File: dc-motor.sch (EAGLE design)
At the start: 60 parts, among them IC1 MEGA8-P, X3 RIA_3POL, X4 RIA_3POL, X5 RIA_2POL, X6 JUMP1-4

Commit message: Schaltplan Fertig
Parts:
- added C15, C16: 15pF, Capacitor:C-BELAB0805
- added H3: MOUNT-HOLE3.2, Holes:MOUNT-HOLE3.2
- added R24, R28, R31, R32: 2k2, Resistor:0805
- added R25, R26, R29, R30: 10R, Resistor:0805
- added R27: 180R, Resistor:0805
- added R33, R34, R35: 2k7, Resistor:0805
- added U$34: ACPL-247, Optoelectronic:ACPL-247
- added U$35, U$38: IRF7341, Transistor:IRF7341
- added X7, X8: PFVERB10, Connector:PFVERB10
- C11: value 1µF -> 100nF
- IC1: value MEGA8-P -> MEGA32-A; device atmel:MEGA8-P -> atmel:MEGA32-A; MPN (none) -> ATMEGA32-16AU; OC_FARNELL (none) -> 9171274; OC_NEWARK (none) -> 69K6677
- R13: value 3,3k -> 2k7
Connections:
- removed net N$14 (its old number): IC1.PC0(ADC0), U$17.OUT
- removed net N$22: IC1.PC6(/RESET), S1.S, S1.S1
- removed net N$30: IC1.PC2(ADC2)
- removed net N$32 (its old number): R21.1, U$3.PHASE
- removed net N$39: IC1.PD4(XCK/T0), R19.1
- removed net N$40: IC1.PD3(INT1), R18.2
- removed net N$41: R17.2
- removed net N$51: IC1.PC3(ADC3)
- removed net N$52: IC1.PC4(ADC4/SDA)
- removed net N$53: IC1.PC5(ADC5/SCL)
- new net ENDLAGE_A: IC1.(T1)PB1, R32.1, U$35G$1.N-G1
- new net ENDLAGE_B: IC1.(T0/XCK)PB0, R31.1, U$35G$2.N-G1
- new net FAEHRTNACHA: IC1.(ADC1)PA1, X7.5.1
- new net FAEHRTNACHB: IC1.(ADC2)PA2, X7.6.1
- new net LOCAL/REMOTE: IC1.(ADC4)PA4, X7.8.1
- new net MISO: IC1.(MISO)PB6, R18.2, X8.3.1
- new net MOSI: IC1.(MOSI)PB5, R19.1, X8.9.1
- new net MOTORSICHERUNGLED: IC1.(ADC0)PA0, X7.4.1
- new net MOTORSTOP: IC1.(ADC3)PA3, X7.7.1
- new net N$10: IC1.(ADC6)PA6, U$17.OUT
- new net N$23: IC1.(AIN1/OC0)PB3, R28.1, U$38G$2.N-G1
- new net N$37: U$34G$2.COL, X2.5
- new net N$54: R26.2, X2.4
- new net N$55: R25.2, X2.3
- new net N$57: U$34G$2.A
- new net N$58: U$34G$2.EMIT, U$38G$1.N-S1, U$38G$2.N-S1
- new net N$59: R25.1, U$38G$2.D1
- new net N$61: R27.2, U$34G$2.C
- new net N$62: R26.1, U$38G$1.D1
- new net N$67: R29.1, X3.1.STIFT
- new net N$68: R30.1, X4.1.STIFT
- new net N$69: R30.2, U$35G$2.D1
- new net N$70: U$35G$2.N-S1, X4.2.STIFT
- new net N$71: R29.2, U$35G$1.D1
- new net N$72: U$35G$1.N-S1, X3.2.STIFT
- new net N$77: R21.1, R35.2, U$3.PHASE
- new net RESET: IC1.RESET, S1.S, S1.S1, X8.6.1
- new net SCK: IC1.(SCK)PB7, R17.2, X8.1.1
- net +24V: now also X7.3.1
- net GND: now also C15.2, C16.2, C3.1, IC1.GND1, IC1.GND2, R13.1, R24.2, R27.1, R28.2, R31.2, R32.2, R33.1, R34.1, R35.1, X3.3.STIFT, X4.3.STIFT, X7.10.1, X8.10.1, X8.2.1
- net N$11: now also IC1.(TMS)PC3; no longer IC1.PB4(MISO)
- net N$15: now also IC1.(TDO)PC4; no longer IC1.PB3(MOSI/OC2)
- net N$16: now also IC1.(AIN0/INT2)PB2, R24.1, U$38G$1.N-G1; no longer C3.1
- net N$17: now also IC1.(TDI)PC5; no longer IC1.PB2(SS/OC1B)
- net N$18: now also IC1.(TOSC1)PC6; no longer IC1.PB1(OC1A)
- net N$19: now also X7.1.1
- net N$2: now also C15.1, G1.1, IC1.XTAL1; no longer G1.2, IC1.PB6(XTAL1/TOSC1)
- net N$20: now also X7.2.1
- net N$21: now also C9.2
- net N$25: now also IC1.(TOSC2)PC7; no longer IC1.PB0(ICP)
- net N$3: now also C16.1, G1.2, IC1.XTAL2; no longer G1.1, IC1.PB7(XTAL2/TOSC2)
- net N$31: now also R34.2
- net N$34: now also R13.2; no longer R13.1
- net N$35: now also R22.2
- net N$38: now also IC1.(SS)PB4; no longer IC1.PD5(T1)
- net N$4: now also IC1.(RXD)PD0; no longer IC1.PD0(RXD)
- net N$48: now also R33.2
- net N$50: now also IC1.(ADC5)PA5; no longer IC1.PC1(ADC1)
- net N$6: now also IC1.(ADC7)PA7
- net N$8: now also IC1.(TXD)PD1; no longer IC1.PD1(TXD)
- net N$9: now also IC1.(TCK)PC2; no longer IC1.PB5(SCK)
- net VDD: now also IC1.VCC, IC1.VCC1, IC1.VCC2, X7.9.1, X8.4.1; no longer IC1.VCC@1, R13.2
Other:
- note added: "Auswertung Endlage A"
- note added: "Auswertung Endlage B"
- note added: "Endschalter A"
- note added: "Endschalter B"
- note added: "Fährt nach A"
- note added: "Fährt nach B"
- note added: "Local/Remote"
- note added: "Motor Sicherung LED"
- note added: "Motorstop"
- moved on the sheet: C10, C2, C3, C4, C7, C8, C9, F1, G1, H1, H2, R10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

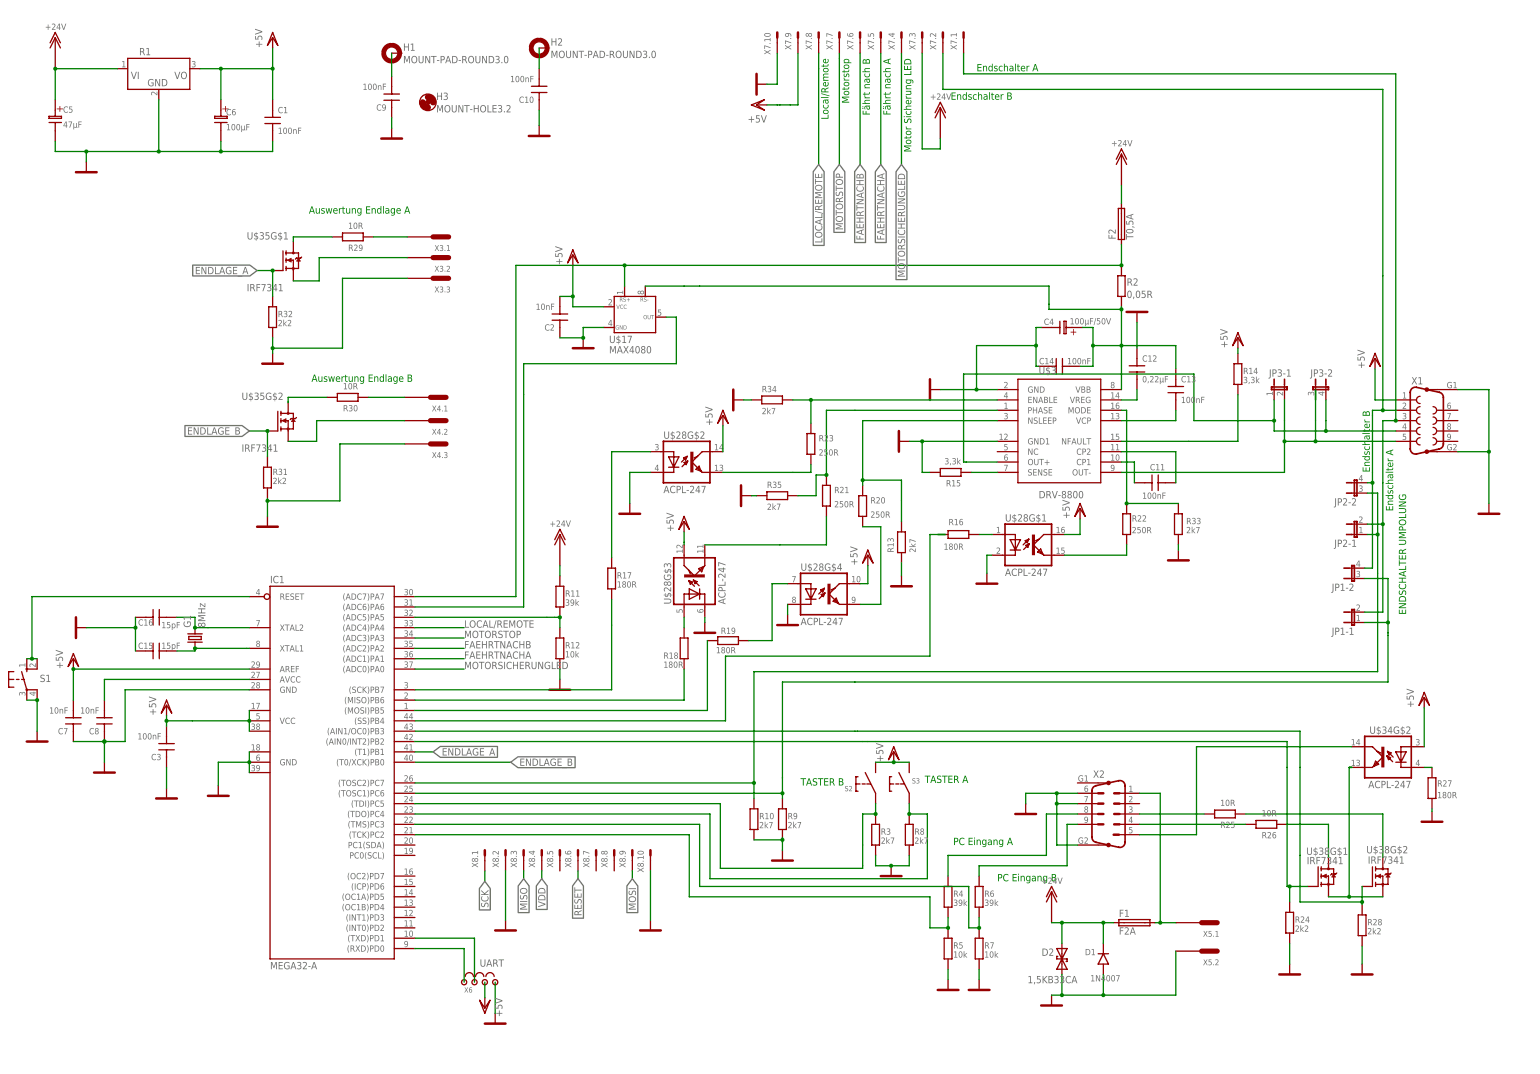
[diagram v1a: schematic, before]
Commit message: Schaltplan Verbessert und mit dem Layout begonnen
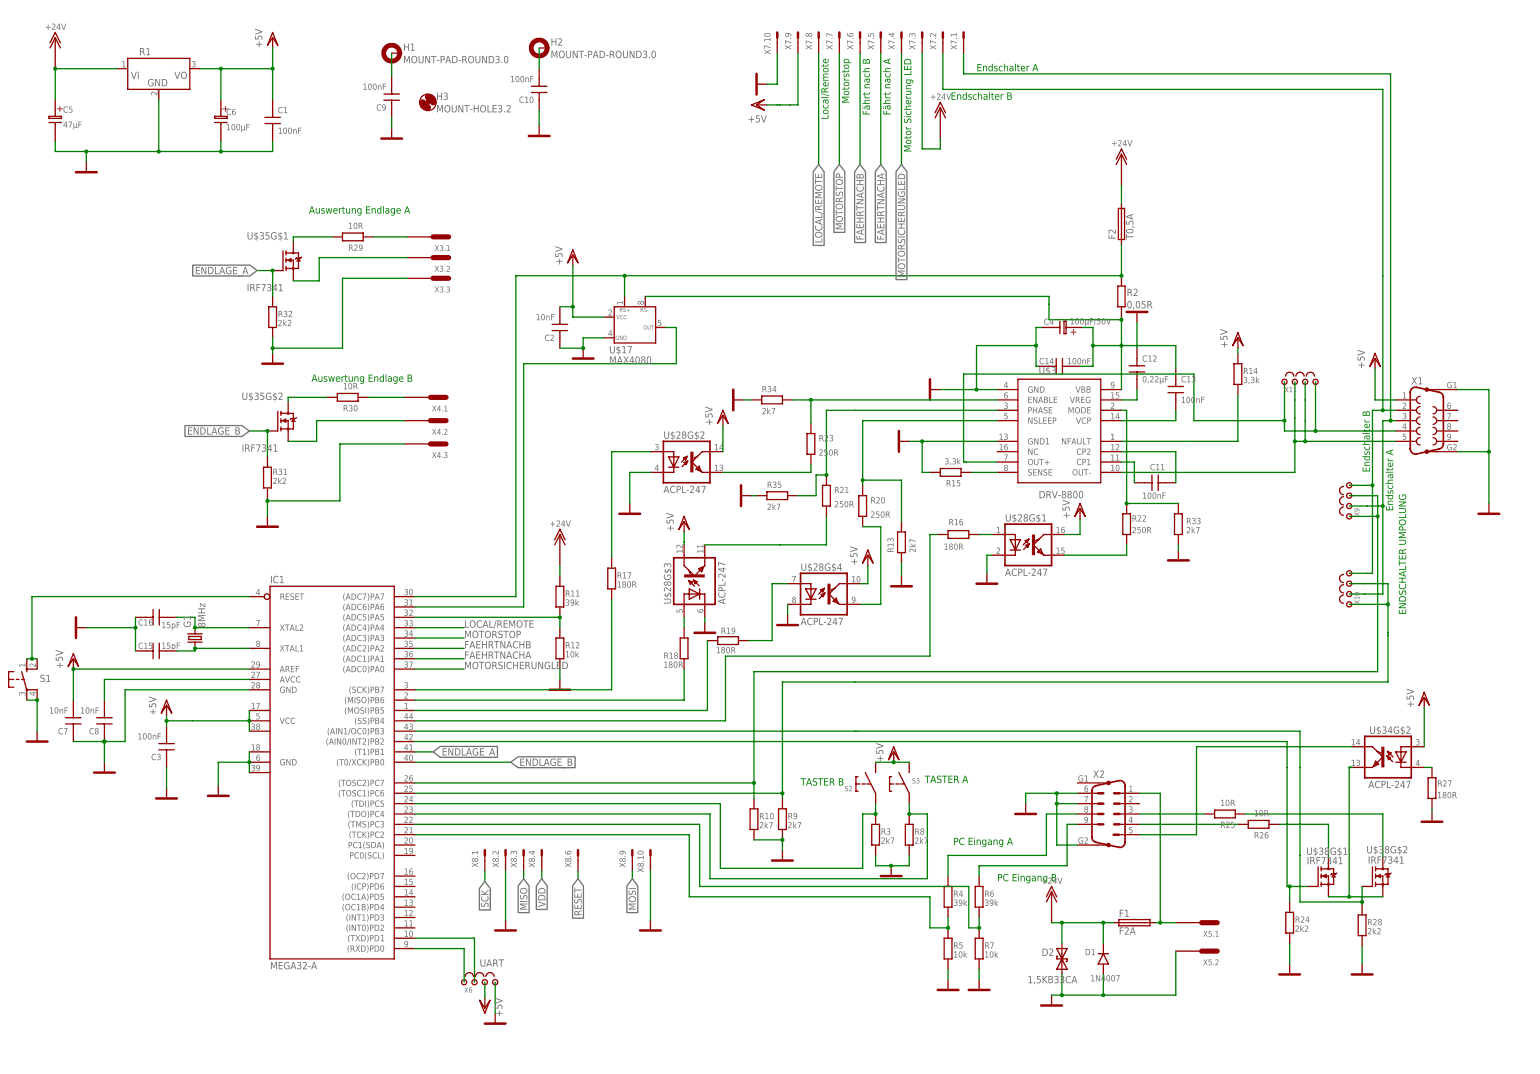
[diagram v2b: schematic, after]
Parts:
- removed JP1, JP2, JP3: (no value), jumper:JP2QE
- added X10, X11, X9: JUMP1-4, Connector:JUMP1-4
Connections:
- removed net N$19 (its old number): JP1-1.2, JP2-1.2, X1.3, X7.1.1
- removed net N$57: U$34G$2.A
- removed net N$7: JP3-1.2, JP3-2.1, U$3.OUT-, X1.5
- new net N$22: X1.3, X10.2, X7.1.1, X9.2
- new net N$30: U$3.OUT-, X1.5, X11.2, X11.3
- net N$18: now also X10.1, X10.3; no longer JP1-1.1, JP1-2.1
- net N$20: now also X10.4, X9.4; no longer JP1-2.2, JP2-2.2
- net N$25: now also X9.1, X9.3; no longer JP2-1.1, JP2-2.1
- net N$5: now also X11.1, X11.4; no longer JP3-1.1, JP3-2.2
- net VDD: now also U$34G$2.A
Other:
- moved on the sheet: C2, R2, R26, U$17

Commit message: Schaltplan erweitert
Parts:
- G1: device Crystals:CRYTAL -> Crystals:CRYTALHC18U-V
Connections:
- net N$6: no longer IC1.(ADC7)PA7
- net VDD: now also IC1.(ADC7)PA7
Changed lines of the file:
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@@
 <setting verticaltext="up"/>
 </settings>
-<grid distance="0.635" unitdist="mm" unit="mm" style="lines" multiple="1" display="yes" altdistance="0.3175" altunitdist="mm" altunit="mm"/>
+<grid distance="0.635" unitdist="mm" unit="mm" style="dots" multiple="1" display="yes" altdistance="0.3175" altunitdist="mm" altunit="mm"/>
 <layers>
-<layer number="1" name="Top" color="4" fill="1" visible="yes" active="no"/>
-<layer number="2" name="Route2" color="1" fill="3" visible="yes" active="no"/>
-<layer number="3" name="Route3" color="4" fill="3" visible="yes" active="no"/>
-<layer number="4" name="Route4" color="1" fill="4" visible="yes" active="no"/>
-<layer number="5" name="Route5" color="4" fill="4" visible="yes" active="no"/>
-<layer number="6" name="Route6" color="1" fill="8" visible="yes" active="no"/>
-<layer number="7" name="Route7" color="4" fill="8" visible="yes" active="no"/>
-<layer number="8" name="Route8" color="1" fill="2" visible="yes" active="no"/>
-<layer number="9" name="Route9" color="4" fill="2" visible="yes" active="no"/>
-<layer number="10" name="Route10" color="1" fill="7" visible="yes" active="no"/>
-<layer number="11" name="Route11" color="4" fill="7" visible="yes" active="no"/>
-<layer number="12" name="Route12" color="1" fill="5" visible="yes" active="no"/>
-<layer number="13" name="Route13" color="4" fill="5" visible="yes" active="no"/>
-<layer number="14" name="Route14" color="1" fill="6" visible="yes" active="no"/>
-<layer number="15" name="Route15" color="4" fill="6" visible="yes" active="no"/>
-<layer number="16" name="Bottom" color="1" fill="1" visible="yes" active="no"/>
-<layer number="17" name="Pads" color="2" fill="1" visible="yes" active="no"/>
-<layer number="18" name="Vias" color="2" fill="1" visible="yes" active="no"/>
-<layer number="19" name="Unrouted" color="6" fill="1" visible="yes" active="no"/>
-<layer number="20" name="Dimension" color="15" fill="1" visible="yes" active="no"/>
-<layer number="21" name="tPlace" color="7" fill="1" visible="yes" active="no"/>
-<layer number="22" name="bPlace" color="7" fill="1" visible="yes" active="no"/>
-<layer number="23" name="tOrigins" color="15" fill="1" visible="yes" active="no"/>
-<layer number="24" name="bOrigins" color="15" fill="1" visible="yes" active="no"/>
-<layer number="25" name="tNames" color="7" fill="1" visible="yes" active="no"/>
-<layer number="26" name="bNames" color="7" fill="1" visible="yes" active="no"/>
-<layer number="27" name="tValues" color="7" fill="1" visible="yes" active="no"/>
-<layer number="28" name="bValues" color="7" fill="1" visible="yes" active="no"/>
+<layer number="1" name="Top" color="4" fill="1" visible="no" active="no"/>
+<layer number="2" name="Route2" color="1" fill="3" visible="no" active="no"/>
+<layer number="3" name="Route3" color="4" fill="3" visible="no" active="no"/>
+<layer number="4" name="Route4" color="1" fill="4" visible="no" active="no"/>
+<layer number="5" name="Route5" color="4" fill="4" visible="no" active="no"/>
+<layer number="6" name="Route6" color="1" fill="8" visible="no" active="no"/>
+<layer number="7" name="Route7" color="4" fill="8" visible="no" active="no"/>
+<layer number="8" name="Route8" color="1" fill="2" visible="no" active="no"/>
+<layer number="9" name="Route9" color="4" fill="2" visible="no" active="no"/>
+<layer number="10" name="Route10" color="1" fill="7" visible="no" active="no"/>
+<layer number="11" name="Route11" color="4" fill="7" visible="no" active="no"/>
+<layer number="12" name="Route12" color="1" fill="5" visible="no" active="no"/>
+<layer number="13" name="Route13" color="4" fill="5" visible="no" active="no"/>
+<layer number="14" name="Route14" color="1" fill="6" visible="no" active="no"/>
+<layer number="15" name="Route15" color="4" fill="6" visible="no" active="no"/>
+<layer number="16" name="Bottom" color="1" fill="1" visible="no" active="no"/>
+<layer number="17" name="Pads" color="2" fill="1" visible="no" active="no"/>
+<layer number="18" name="Vias" color="2" fill="1" visible="no" active="no"/>
+<layer number="19" name="Unrouted" color="6" fill="1" visible="no" active="no"/>
+<layer number="20" name="Dimension" color="15" fill="1" visible="no" active="no"/>
+<layer number="21" name="tPlace" color="7" fill="1" visible="no" active="no"/>
+<layer number="22" name="bPlace" color="7" fill="1" visible="no" active="no"/>
+<layer number="23" name="tOrigins" color="15" fill="1" visible="no" active="no"/>
+<layer number="24" name="bOrigins" color="15" fill="1" visible="no" active="no"/>
+<layer number="25" name="tNames" color="7" fill="1" visible="no" active="no"/>
+<layer number="26" name="bNames" color="7" fill="1" visible="no" active="no"/>
+<layer number="27" name="tValues" color="7" fill="1" visible="no" active="no"/>
+<layer number="28" name="bValues" color="7" fill="1" visible="no" active="no"/>
 <layer number="29" name="tStop" color="7" fill="3" visible="no" active="no"/>
 <layer number="30" name="bStop" color="7" fill="6" visible="no" active="no"/>
@@
 <layer number="35" name="tGlue" color="7" fill="4" visible="no" active="no"/>
 <layer number="36" name="bGlue" color="7" fill="5" visible="no" active="no"/>
-<layer number="37" name="tTest" color="7" fill="1" visible="yes" active="no"/>
-<layer number="38" name="bTest" color="7" fill="1" visible="yes" active="no"/>
+<layer number="37" name="tTest" color="7" fill="1" visible="no" active="no"/>
+<layer number="38" name="bTest" color="7" fill="1" visible="no" active="no"/>
 <layer number="39" name="tKeepout" color="4" fill="11" visible="no" active="no"/>
 <layer number="40" name="bKeepout" color="1" fill="11" visible="no" active="no"/>
@@
 <layer number="44" name="Drills" color="7" fill="1" visible="no" active="no"/>
 <layer number="45" name="Holes" color="7" fill="1" visible="no" active="no"/>
-<layer number="46" name="Milling" color="3" fill="1" visible="yes" active="no"/>
-<layer number="47" name="Measures" color="7" fill="1" visible="yes" active="no"/>
-<layer number="48" name="Document" color="7" fill="1" visible="yes" active="no"/>
-<layer number="49" name="Reference" color="7" fill="1" visible="yes" active="no"/>
-<layer number="50" name="dxf" color="7" fill="1" visible="yes" active="no"/>
-<layer number="51" name="tDocu" color="7" fill="1" visible="yes" active="no"/>
-<layer number="52" name="bDocu" color="7" fill="1" visible="yes" active="no"/>
-<layer number="56" name="wert" color="7" fill="1" visible="yes" active="no"/>
+<layer number="46" name="Milling" color="3" fill="1" visible="no" active="no"/>
+<layer number="47" name="Measures" color="7" fill="1" visible="no" active="no"/>
+<layer number="48" name="Document" color="7" fill="1" visible="no" active="no"/>
+<layer number="49" name="Reference" color="7" fill="1" visible="no" active="no"/>
+<layer number="50" name="dxf" color="7" fill="1" visible="no" active="no"/>
+<layer number="51" name="tDocu" color="7" fill="1" visible="no" active="no"/>
+<layer number="52" name="bDocu" color="7" fill="1" visible="no" active="no"/>
+<layer number="56" name="wert" color="7" fill="1" visible="no" active="no"/>
 <layer number="91" name="Nets" color="2" fill="1" visible="yes" active="yes"/>
 <layer number="92" name="Busses" color="1" fill="1" visible="yes" active="yes"/>
@@
 <part name="X5" library="Connector" deviceset="RIA_2POL" device=""/>
 <part name="U$3" library="DRV-8800" deviceset="DRV-8800" device=""/>
-<part name="G1" library="Crystals" deviceset="CRYTAL" device="" value="8MHz"/>
+<part name="G1" library="Crystals" deviceset="CRYTAL" device="HC18U-V" value="8MHz"/>
 <part name="X6" library="Connector" deviceset="JUMP1-4" device=""/>
 <part name="U$7" library="PowerSupply" deviceset="+24V" device=""/>
@@
 <part name="X10" library="Connector" deviceset="JUMP1-4" device=""/>
 <part name="X11" library="Connector" deviceset="JUMP1-4" device=""/>
+<part name="VDD8" library="supply1" deviceset="VDD" device="" value="+5V"/>
 </parts>
 <sheets>
@@
 <instance part="X10" gate="G$1" x="335.28" y="127.635" rot="R90"/>
 <instance part="X11" gate="G$1" x="321.945" y="179.705"/>
+<instance part="VDD8" gate="G$1" x="113.665" y="133.35"/>
 </instances>
 <busses>
@@
 <pinref part="U$34" gate="G$2" pin="A"/>
 <wire x1="353.695" y1="99.695" x2="353.695" y2="90.17" width="0.1524" layer="91"/>
+</segment>
+<segment>
+<pinref part="IC1" gate="G$1" pin="(ADC7)PA7"/>
+<pinref part="VDD8" gate="G$1" pin="VDD"/>
+<wire x1="106.045" y1="127" x2="113.665" y2="127" width="0.1524" layer="91"/>
+<wire x1="113.665" y1="127" x2="113.665" y2="130.81" width="0.1524" layer="91"/>
 </segment>
 </net>
@@
 <pinref part="U$17" gate="G$1" pin="RS+"/>
 <wire x1="157.48" y1="205.74" x2="157.48" y2="200.66" width="0.1524" layer="91"/>
-<wire x1="157.48" y1="205.74" x2="130.81" y2="205.74" width="0.1524" layer="91"/>
-<wire x1="130.81" y1="205.74" x2="130.81" y2="127" width="0.1524" layer="91"/>
-<junction x="157.48" y="205.74"/>
-<pinref part="IC1" gate="G$1" pin="(ADC7)PA7"/>
-<wire x1="106.045" y1="127" x2="130.81" y2="127" width="0.1524" layer="91"/>
 </segment>
 </net>
